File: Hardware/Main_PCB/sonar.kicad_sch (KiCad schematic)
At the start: 12 parts, among them J201 Conn_01x03_Pin, U4 TUSS4470TRTJT

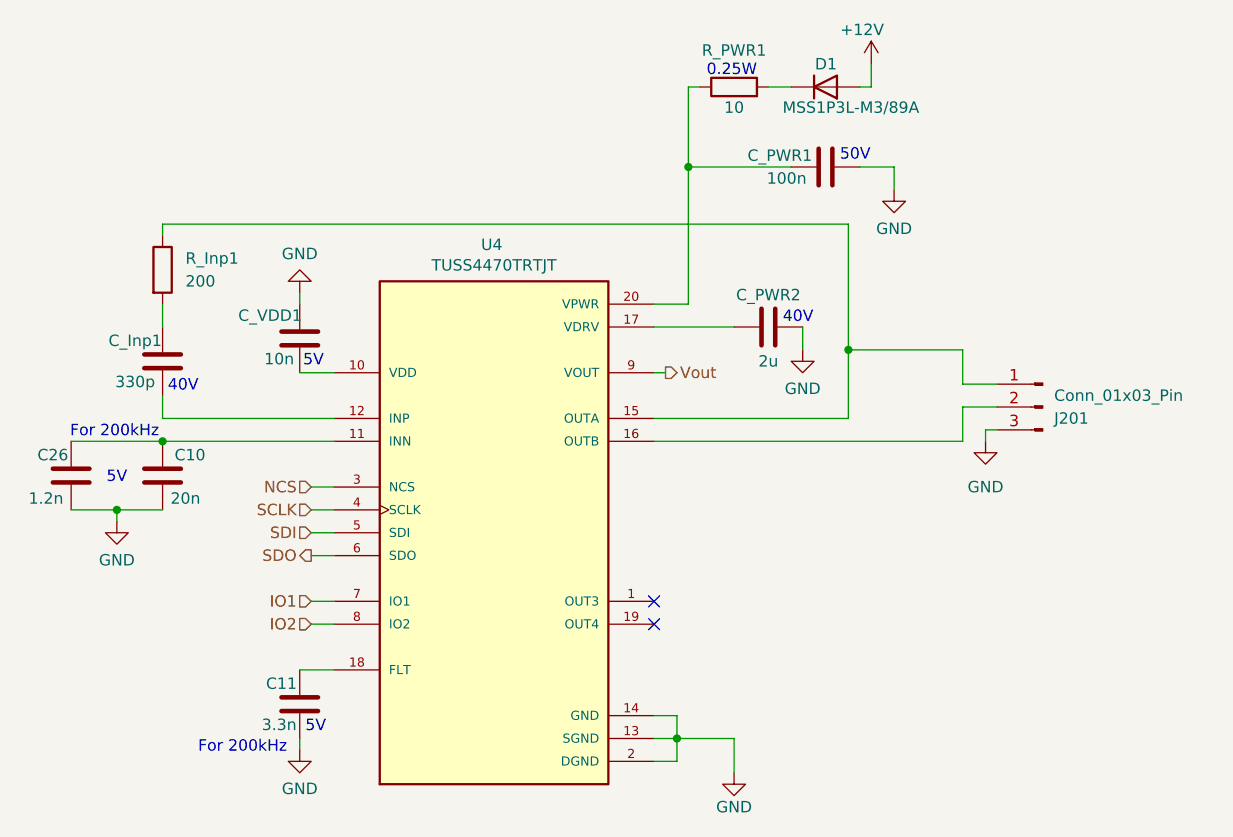
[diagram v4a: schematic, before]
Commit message: A finished version of the Main PCB schematic
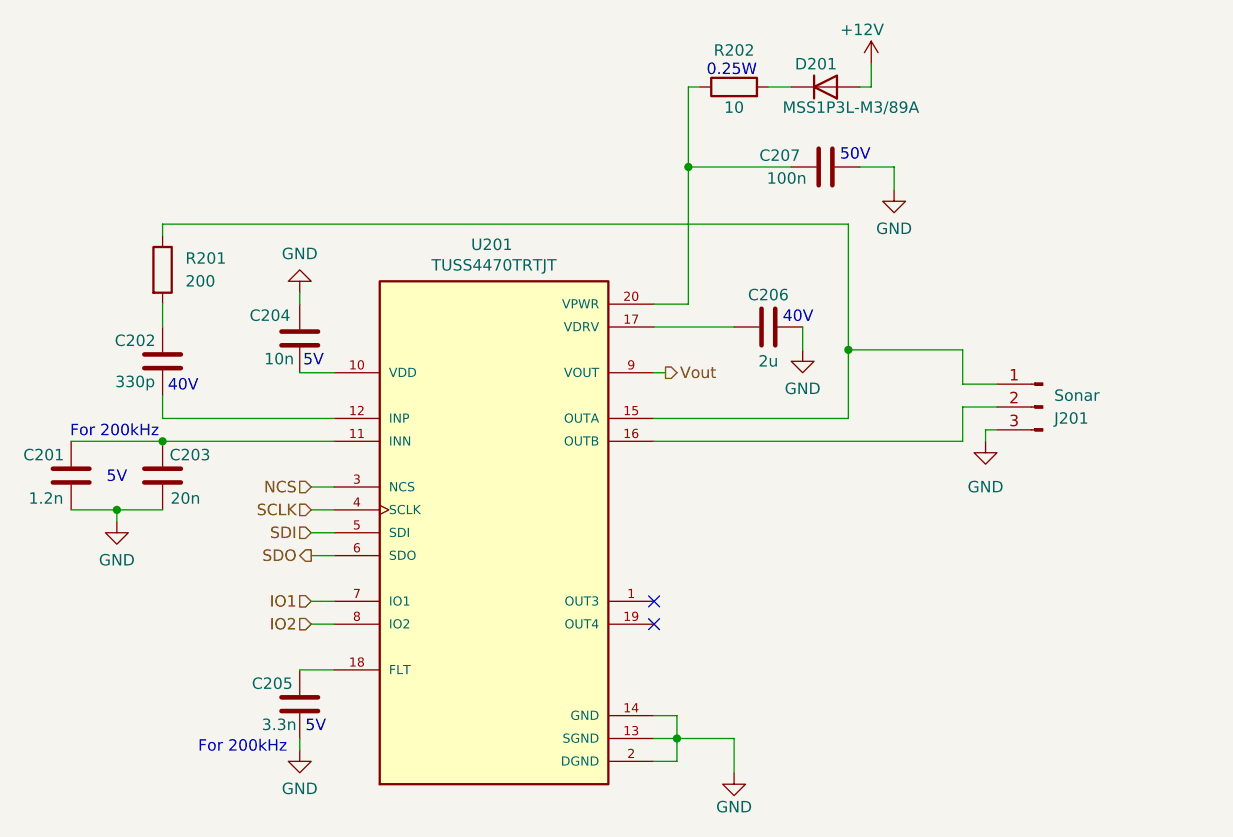
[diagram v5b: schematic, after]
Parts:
- J201: value Conn_01x03_Pin -> Sonar
- renumbered C26 to C201, C_Inp1 to C202, C10 to C203, C_VDD1 to C204, C11 to C205, C_PWR2 to C206, C_PWR1 to C207, D1 to D201, R_Inp1 to R201, R_PWR1 to R202, U4 to U201
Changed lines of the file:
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@@
 		(on_board yes)
 		(dnp no)
-		(property "Reference" "#PWR01"
+		(property "Reference" "#PWR0206"
 			(at 133.35 22.86 0)
 			(effects
@@
 			(project "Main_PCB"
 				(path "/90d7beec-e1a2-46f8-bbb2-6b8f3489db10/fb18f23d-afe6-46fa-a762-d7c19ead7543"
-					(reference "#PWR01")
+					(reference "#PWR0206")
 					(unit 1)
 				)
@@
 		(on_board yes)
 		(dnp no)
-		(property "Reference" "#PWR05"
+		(property "Reference" "#PWR0201"
 			(at 49.53 76.2 0)
 			(effects
@@
 			(project "Main_PCB"
 				(path "/90d7beec-e1a2-46f8-bbb2-6b8f3489db10/fb18f23d-afe6-46fa-a762-d7c19ead7543"
-					(reference "#PWR05")
+					(reference "#PWR0201")
 					(unit 1)
 				)
@@
 		(on_board yes)
 		(dnp no)
-		(property "Reference" "#PWR04"
+		(property "Reference" "#PWR0205"
 			(at 125.73 57.15 0)
 			(effects
@@
 			(project "Main_PCB"
 				(path "/90d7beec-e1a2-46f8-bbb2-6b8f3489db10/fb18f23d-afe6-46fa-a762-d7c19ead7543"
-					(reference "#PWR04")
+					(reference "#PWR0205")
 					(unit 1)
 				)
@@
 		(on_board yes)
 		(dnp no)
-		(property "Reference" "#PWR08"
+		(property "Reference" "#PWR0204"
 			(at 118.11 104.14 0)
 			(effects
@@
 			(project "Main_PCB"
 				(path "/90d7beec-e1a2-46f8-bbb2-6b8f3489db10/fb18f23d-afe6-46fa-a762-d7c19ead7543"
-					(reference "#PWR08")
+					(reference "#PWR0204")
 					(unit 1)
 				)
@@
 		(on_board yes)
 		(dnp no)
-		(property "Reference" "U4"
+		(property "Reference" "U201"
 			(at 91.186 39.116 0)
 			(effects
@@
 			(project "Main_PCB"
 				(path "/90d7beec-e1a2-46f8-bbb2-6b8f3489db10/fb18f23d-afe6-46fa-a762-d7c19ead7543"
-					(reference "U4")
+					(reference "U201")
 					(unit 1)
 				)
@@
 		(on_board yes)
 		(dnp no)
-		(property "Reference" "#PWR03"
+		(property "Reference" "#PWR0202"
 			(at 69.85 38.1 0)
 			(effects
@@
 			(project "Main_PCB"
 				(path "/90d7beec-e1a2-46f8-bbb2-6b8f3489db10/fb18f23d-afe6-46fa-a762-d7c19ead7543"
-					(reference "#PWR03")
+					(reference "#PWR0202")
 					(unit 1)
 				)
@@
 		(on_board yes)
 		(dnp no)
-		(property "Reference" "#PWR02"
+		(property "Reference" "#PWR0207"
 			(at 135.89 39.37 0)
 			(effects
@@
 			(project "Main_PCB"
 				(path "/90d7beec-e1a2-46f8-bbb2-6b8f3489db10/fb18f23d-afe6-46fa-a762-d7c19ead7543"
-					(reference "#PWR02")
+					(reference "#PWR0207")
 					(unit 1)
 				)
@@
 		(on_board yes)
 		(dnp no)
-		(property "Reference" "C11"
-			(at 67.818 87.884 0)
+		(property "Reference" "C205"
+			(at 66.802 87.884 0)
 			(effects
 				(font
@@
 			(project "Main_PCB"
 				(path "/90d7beec-e1a2-46f8-bbb2-6b8f3489db10/fb18f23d-afe6-46fa-a762-d7c19ead7543"
-					(reference "C11")
+					(reference "C205")
 					(unit 1)
 				)
@@
 		(on_board yes)
 		(dnp no)
-		(property "Reference" "R_PWR1"
+		(property "Reference" "R202"
 			(at 118.11 17.526 90)
 			(effects
@@
 			(project "Main_PCB"
 				(path "/90d7beec-e1a2-46f8-bbb2-6b8f3489db10/fb18f23d-afe6-46fa-a762-d7c19ead7543"
-					(reference "R_PWR1")
+					(reference "R202")
 					(unit 1)
 				)
@@
 		(on_board yes)
 		(dnp no)
-		(property "Reference" "C_PWR1"
+		(property "Reference" "C207"
 			(at 123.19 29.21 90)
 			(effects
@@
 			(project "Main_PCB"
 				(path "/90d7beec-e1a2-46f8-bbb2-6b8f3489db10/fb18f23d-afe6-46fa-a762-d7c19ead7543"
-					(reference "C_PWR1")
+					(reference "C207")
 					(unit 1)
 				)
@@
 			)
 		)
-		(property "Value" "Conn_01x03_Pin"
+		(property "Value" "Sonar"
 			(at 153.67 55.8801 0)
 			(effects
@@
 		(dnp no)
 		(fields_autoplaced yes)
-		(property "Reference" "R_Inp1"
+		(property "Reference" "R201"
 			(at 57.15 40.6399 0)
 			(effects
@@
 			(project "Main_PCB"
 				(path "/90d7beec-e1a2-46f8-bbb2-6b8f3489db10/fb18f23d-afe6-46fa-a762-d7c19ead7543"
-					(reference "R_Inp1")
+					(reference "R201")
 					(unit 1)
 				)
@@
 		(on_board yes)
 		(dnp no)
-		(property "Reference" "C_PWR2"
+		(property "Reference" "C206"
 			(at 121.92 44.704 90)
 			(effects
@@
 			(project "Main_PCB"
 				(path "/90d7beec-e1a2-46f8-bbb2-6b8f3489db10/fb18f23d-afe6-46fa-a762-d7c19ead7543"
-					(reference "C_PWR2")
+					(reference "C206")
 					(unit 1)
 				)
@@
 		(on_board yes)
 		(dnp no)
-		(property "Reference" "C_VDD1"
+		(property "Reference" "C204"
 			(at 66.548 46.99 0)
 			(effects
@@
 			(project "Main_PCB"
 				(path "/90d7beec-e1a2-46f8-bbb2-6b8f3489db10/fb18f23d-afe6-46fa-a762-d7c19ead7543"
-					(reference "C_VDD1")
+					(reference "C204")
 					(unit 1)
 				)
@@
 		(on_board yes)
 		(dnp no)
-		(property "Reference" "C26"
-			(at 42.418 62.484 0)
+		(property "Reference" "C201"
+			(at 41.402 62.484 0)
 			(effects
 				(font
@@
 			(project "Main_PCB"
 				(path "/90d7beec-e1a2-46f8-bbb2-6b8f3489db10/fb18f23d-afe6-46fa-a762-d7c19ead7543"
-					(reference "C26")
+					(reference "C201")
 					(unit 1)
 				)
@@
 		(dnp no)
 		(fields_autoplaced yes)
-		(property "Reference" "#PWR0201"
+		(property "Reference" "#PWR0208"
 			(at 146.05 67.31 0)
 			(effects
@@
 			(project ""
 				(path "/90d7beec-e1a2-46f8-bbb2-6b8f3489db10/fb18f23d-afe6-46fa-a762-d7c19ead7543"
-					(reference "#PWR0201")
+					(reference "#PWR0208")
 					(unit 1)
 				)
@@
 		(on_board yes)
 		(dnp no)
-		(property "Reference" "C_Inp1"
+		(property "Reference" "C202"
 			(at 51.562 49.784 0)
 			(effects
@@
 			(project "Main_PCB"
 				(path "/90d7beec-e1a2-46f8-bbb2-6b8f3489db10/fb18f23d-afe6-46fa-a762-d7c19ead7543"
-					(reference "C_Inp1")
+					(reference "C202")
 					(unit 1)
 				)
@@
 		(on_board yes)
 		(dnp no)
-		(property "Reference" "C10"
+		(property "Reference" "C203"
 			(at 57.658 62.484 0)
 			(effects
@@
 			(project "Main_PCB"
 				(path "/90d7beec-e1a2-46f8-bbb2-6b8f3489db10/fb18f23d-afe6-46fa-a762-d7c19ead7543"
-					(reference "C10")
+					(reference "C203")
 					(unit 1)
 				)
@@
 		(on_board yes)
 		(dnp no)
-		(property "Reference" "#PWR06"
+		(property "Reference" "#PWR0203"
 			(at 69.85 101.6 0)
 			(effects
@@
 			(project "Main_PCB"
 				(path "/90d7beec-e1a2-46f8-bbb2-6b8f3489db10/fb18f23d-afe6-46fa-a762-d7c19ead7543"
-					(reference "#PWR06")
+					(reference "#PWR0203")
 					(unit 1)
 				)
@@
 		(on_board yes)
 		(dnp no)
-		(property "Reference" "D1"
+		(property "Reference" "D201"
 			(at 129.5401 19.05 0)
 			(effects
@@
 			(project "Main_PCB"
 				(path "/90d7beec-e1a2-46f8-bbb2-6b8f3489db10/fb18f23d-afe6-46fa-a762-d7c19ead7543"
-					(reference "D1")
-					(unit 1)
-				)
+					(reference "D201")
+					(unit 1)
+				)

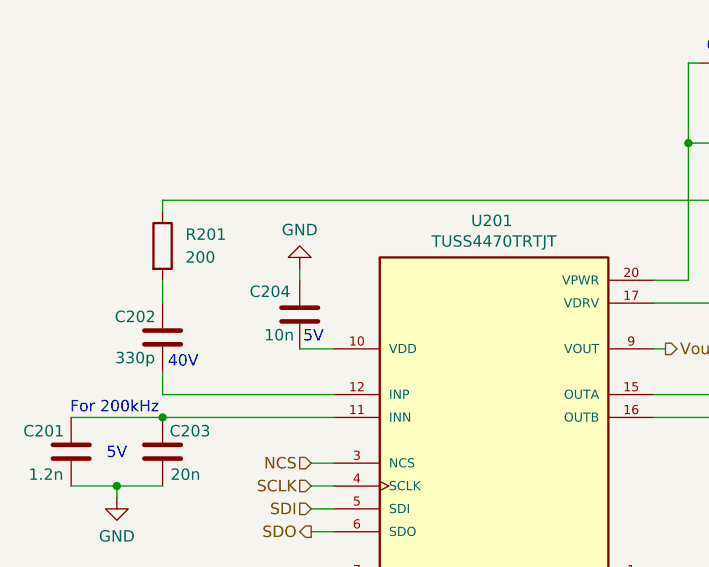
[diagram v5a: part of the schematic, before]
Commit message: Added footprints to all components
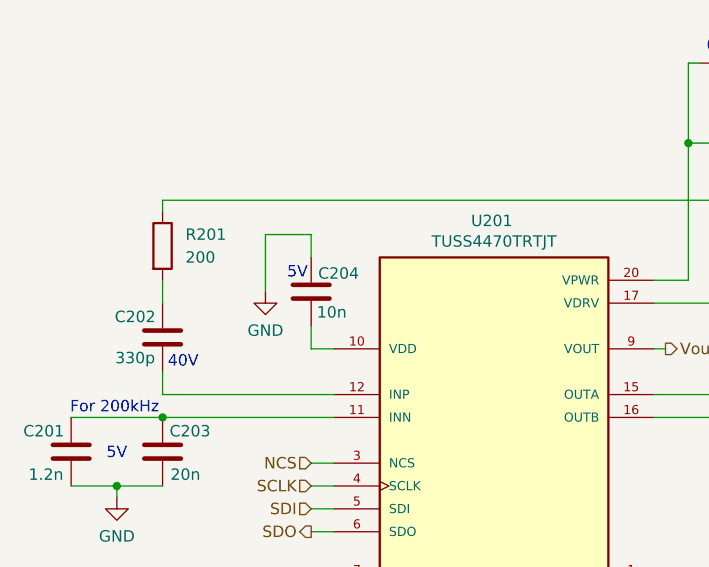
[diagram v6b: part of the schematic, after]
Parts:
- R201: footprint (none) -> Resistor_SMD:R_0603_1608Metric_Pad0.98x0.95mm_HandSolder
- U201: footprint TUSS4470TRTJT:QFN50P400X400X80-21N -> MainPCB:QFN50P400X400X80-21N
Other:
- moved on the sheet: C204
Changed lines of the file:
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@@
 	(text "5V"
 		(exclude_from_sim no)
-		(at 71.374 52.07 0)
+		(at 69.596 44.958 0)
 		(effects
 			(font
@@
 	(wire
 		(pts
+			(xy 71.12 53.34) (xy 73.66 53.34)
+		)
+		(stroke
+			(width 0)
+			(type default)
+		)
+	)
+	(wire
+		(pts
 			(xy 143.51 50.8) (xy 143.51 54.61)
 		)
@@
 	(wire
 		(pts
-			(xy 69.85 53.34) (xy 73.66 53.34)
-		)
-		(stroke
-			(width 0)
-			(type default)
-		)
-	)
-	(wire
-		(pts
 			(xy 111.76 93.98) (xy 111.76 96.52)
 		)
@@
 	(wire
 		(pts
-			(xy 69.85 44.45) (xy 69.85 45.72)
-		)
-		(stroke
-			(width 0)
-			(type default)
-		)
-	)
-	(wire
-		(pts
 			(xy 113.03 21.59) (xy 114.3 21.59)
 		)
@@
 	(wire
 		(pts
+			(xy 71.12 40.64) (xy 71.12 43.18)
+		)
+		(stroke
+			(width 0)
+			(type default)
+		)
+	)
+	(wire
+		(pts
 			(xy 121.92 21.59) (xy 124.46 21.59)
 		)
@@
 	(wire
 		(pts
+			(xy 71.12 50.8) (xy 71.12 53.34)
+		)
+		(stroke
+			(width 0)
+			(type default)
+		)
+	)
+	(wire
+		(pts
 			(xy 130.81 58.42) (xy 130.81 50.8)
 		)
@@
 	(wire
 		(pts
+			(xy 66.04 46.99) (xy 66.04 40.64)
+		)
+		(stroke
+			(width 0)
+			(type default)
+		)
+	)
+	(wire
+		(pts
 			(xy 130.81 50.8) (xy 143.51 50.8)
 		)
@@
 		(pts
 			(xy 71.12 66.04) (xy 73.66 66.04)
+		)
+		(stroke
+			(width 0)
+			(type default)
+		)
+	)
+	(wire
+		(pts
+			(xy 66.04 40.64) (xy 71.12 40.64)
 		)
 		(stroke
@@
 			)
 		)
-		(property "Footprint" "TUSS4470TRTJT:QFN50P400X400X80-21N"
+		(property "Footprint" "MainPCB:QFN50P400X400X80-21N"
 			(at 91.44 71.12 0)
 			(effects
@@
 	(symbol
 		(lib_id "power:GND")
-		(at 69.85 44.45 180)
+		(at 66.04 46.99 0)
 		(unit 1)
 		(exclude_from_sim no)
@@
 		(dnp no)
 		(property "Reference" "#PWR0202"
-			(at 69.85 38.1 0)
+			(at 66.04 53.34 0)
 			(effects
 				(font
@@
 		)
 		(property "Value" "GND"
-			(at 69.85 40.132 0)
+			(at 66.04 51.308 0)
 			(effects
 				(font
@@
 		)
 		(property "Footprint" ""
-			(at 69.85 44.45 0)
+			(at 66.04 46.99 0)
 			(effects
 				(font
@@
 		)
 		(property "Datasheet" ""
-			(at 69.85 44.45 0)
+			(at 66.04 46.99 0)
 			(effects
 				(font
@@
 		)
 		(property "Description" "Power symbol creates a global label with name \"GND\" , ground"
-			(at 69.85 44.45 0)
+			(at 66.04 46.99 0)
 			(effects
 				(font
@@
 			)
 		)
-		(property "Footprint" ""
+		(property "Footprint" "Resistor_SMD:R_0603_1608Metric_Pad0.98x0.95mm_HandSolder"
 			(at 52.832 41.91 90)
 			(effects
@@
 	(symbol
 		(lib_id "Device:C")
-		(at 69.85 49.53 180)
+		(at 71.12 46.99 180)
 		(unit 1)
 		(exclude_from_sim no)
@@
 		(dnp no)
 		(property "Reference" "C204"
-			(at 66.548 46.99 0)
+			(at 74.168 44.958 0)
 			(effects
 				(font
@@
 		)
 		(property "Value" "10n"
-			(at 67.564 51.816 0)
+			(at 73.406 49.276 0)
 			(effects
 				(font
@@
 		)
 		(property "Footprint" "Capacitor_SMD:C_0805_2012Metric_Pad1.18x1.45mm_HandSolder"
-			(at 68.8848 45.72 0)
+			(at 70.1548 43.18 0)
 			(effects
 				(font
@@
 		)
 		(property "Datasheet" "~"
-			(at 69.85 49.53 0)
+			(at 71.12 46.99 0)
 			(effects
 				(font
@@
 		)
 		(property "Description" "Unpolarized capacitor"
-			(at 69.85 49.53 0)
-			(effects
-				(font
+			(at 71.12 46.99 0)
+			(effects
+				(font

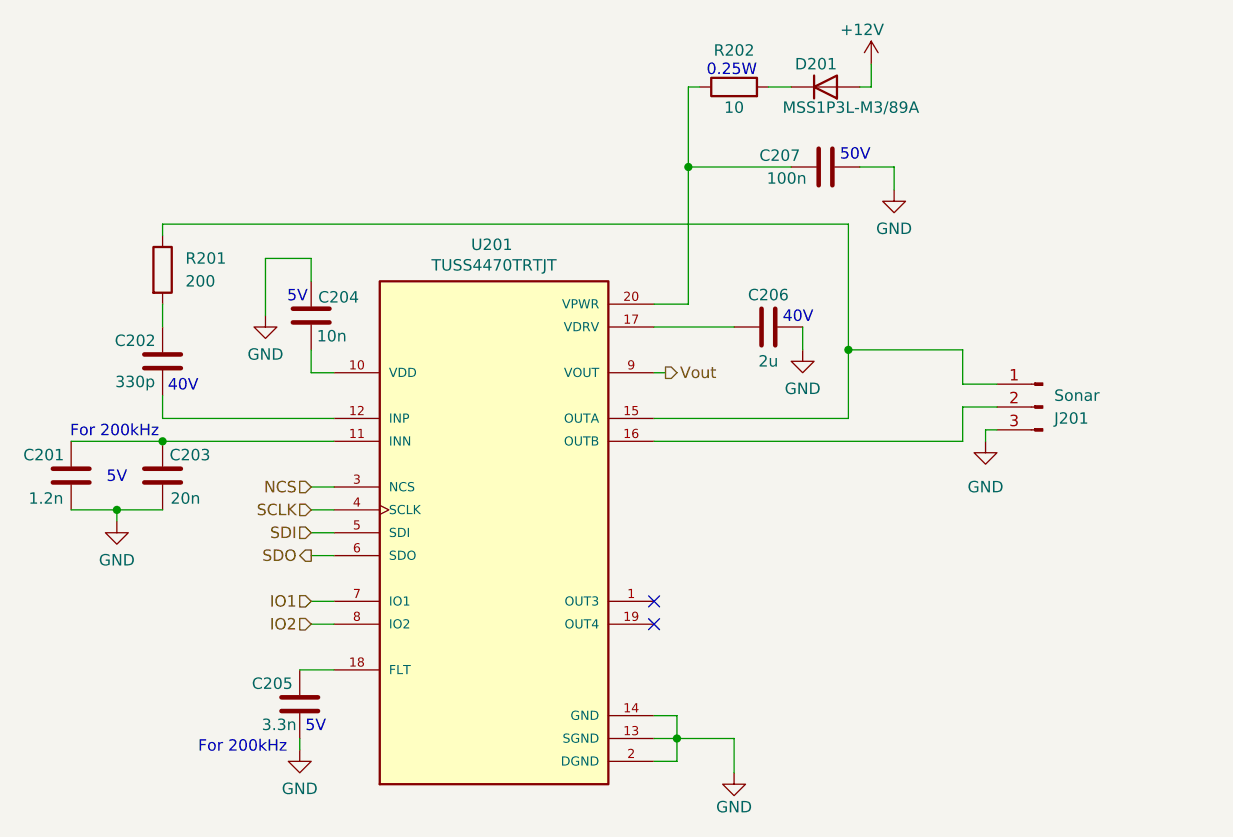
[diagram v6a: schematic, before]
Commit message: Finished the schematic of the MainPCB
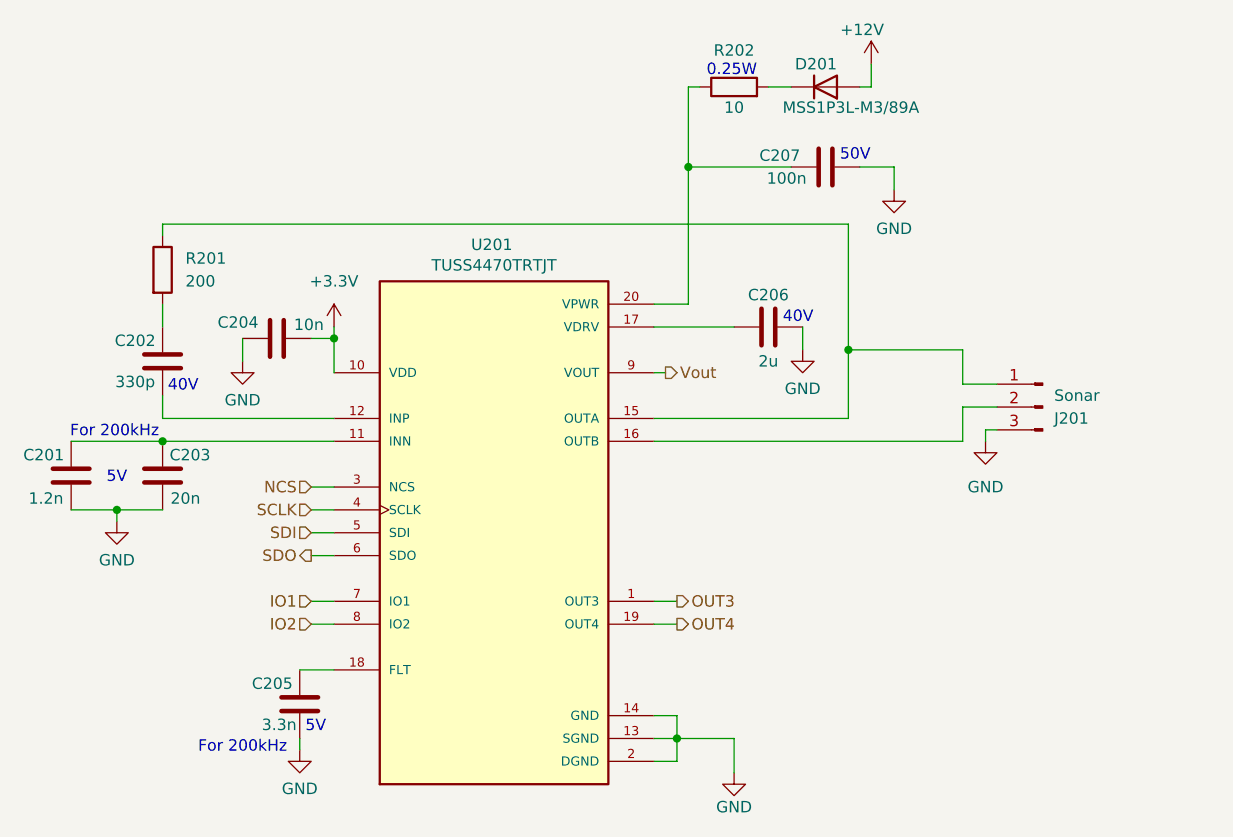
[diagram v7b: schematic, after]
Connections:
- net OUT3: now reaches U201.1 (OUT3)
- net +3.3V: now reaches C204.1, U201.10 (VDD)
- net OUT4: now reaches U201.19 (OUT4)
- no-connect marks 2 -> 0
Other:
- moved on the sheet: C204

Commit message: V1.1 of the MainPCB
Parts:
- added C208: 1u, Capacitor_SMD:C_0603_1608Metric_Pad1.08x0.95mm_HandSolder, symbol Device:C
- C203: value 20n -> 22n; footprint Capacitor_SMD:C_0805_2012Metric_Pad1.18x1.45mm_HandSolder -> Capacitor_SMD:C_0603_1608Metric_Pad1.08x0.95mm_HandSolder
- C206: value 2u -> 1u
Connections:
- net GND: now also C206.1, C208.1; no longer C206.2
- net at U201.17 (VDRV): now also C206.2, C208.2; no longer C206.1
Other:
- moved on the sheet: C206, J201
